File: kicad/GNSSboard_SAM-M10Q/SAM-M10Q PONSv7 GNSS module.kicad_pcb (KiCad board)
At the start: 2 copper layers, 34 x 16 mm, 8 parts, among them J1 2005280040, U2 SAM-M10Q-00B

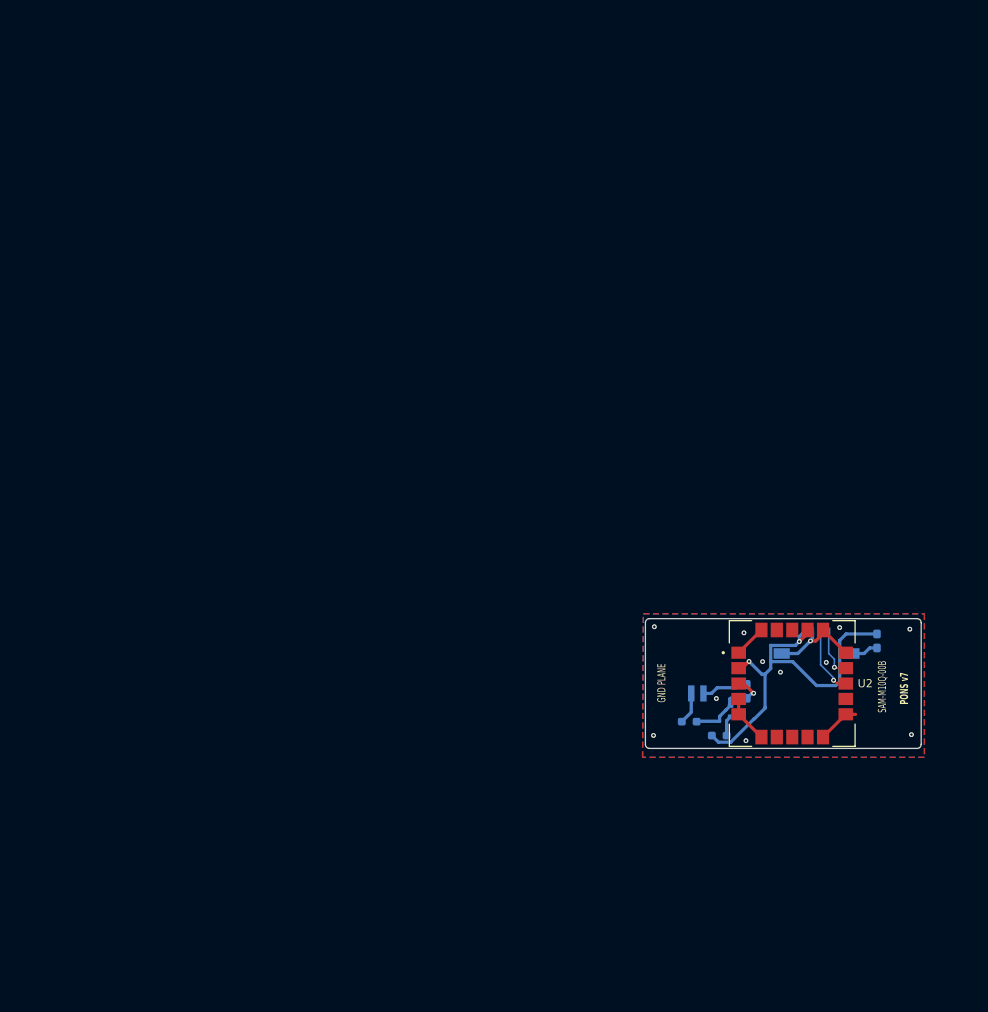
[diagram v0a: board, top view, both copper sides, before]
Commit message: 0.986 新基板（SCH16T 外付け）の kicad を追加し、ガーバー出力を git から外した
kicad/IMU_murata/ — SCH16T-K01-10 のブレイクアウト（新規）
本体の J7（Molex 200528-0080・8pin FPC）へ 1:1 ケーブルで繋ぐ外付け基板。
J1 のピン順を本体 J7 と一致させてある（1=+3V3 2=RESET 3=MOSI 4=CS 5=SCK
6=SYNC 7=MISO 8=GND）。シンボルとフットプリントも同梱。
- ★ R2（CS-GND の 4.7k）は実装しない。CS は負論理なので、プルダウンすると
  MCU が駆動していない間セレクト状態になる。R1（EXTRESN プルアップ）は実装する
- 本体側の GPIO 割り当ては settings.h の SCH16T_PIN_* が正本
  （一覧は docs/imu_sch16t_plan.md §3）

mainboard / GNSS モジュールの更新
- mainboard: DisplayModule_PONSv7 の pcb / pro / sch、MS5611BNO085.kicad_sch、
  SHT_RP2354B.kicad_sch
- GNSS モジュール: pcb / pro / sch、および QRv7 と FPC 4p のフットプリントを
  同プロジェクトの Footprints/ へ取り込み

kicad/FPC/ を畳んだ
FPC コネクタ 1 個のためのプロジェクトだったので、フットプリントを
kicad/GNSSboard_SAM-M10Q/Footprints/ へ移して削除した。
中身は同じで、差分は KiCad が再生成する uuid だけ。

ガーバー・ドリルのプロット出力を git から外した
kicad/.gitignore に追加（*.gbr *.gbl *.gbs *.gbp *.gbo *.gm1 *.gtl *.gts
*.gtp *.gto *.drl と、保険の *plot/ *plot.zip）。発注のたびに作り直せるうえ、
基板を直すたびに巨大な差分になる（ルート .gitignore の production/ と同じ理由）。
★ 入れ物のフォルダ名で書かないこと。v5_1plot/ のような名前は付け方が毎回違うので
  次の基板で外れる。既存の *-backups/ / *.kicad_prl と同じ方針。

Co-Authored-By: Claude Opus 5 <noreply@anthropic.com>
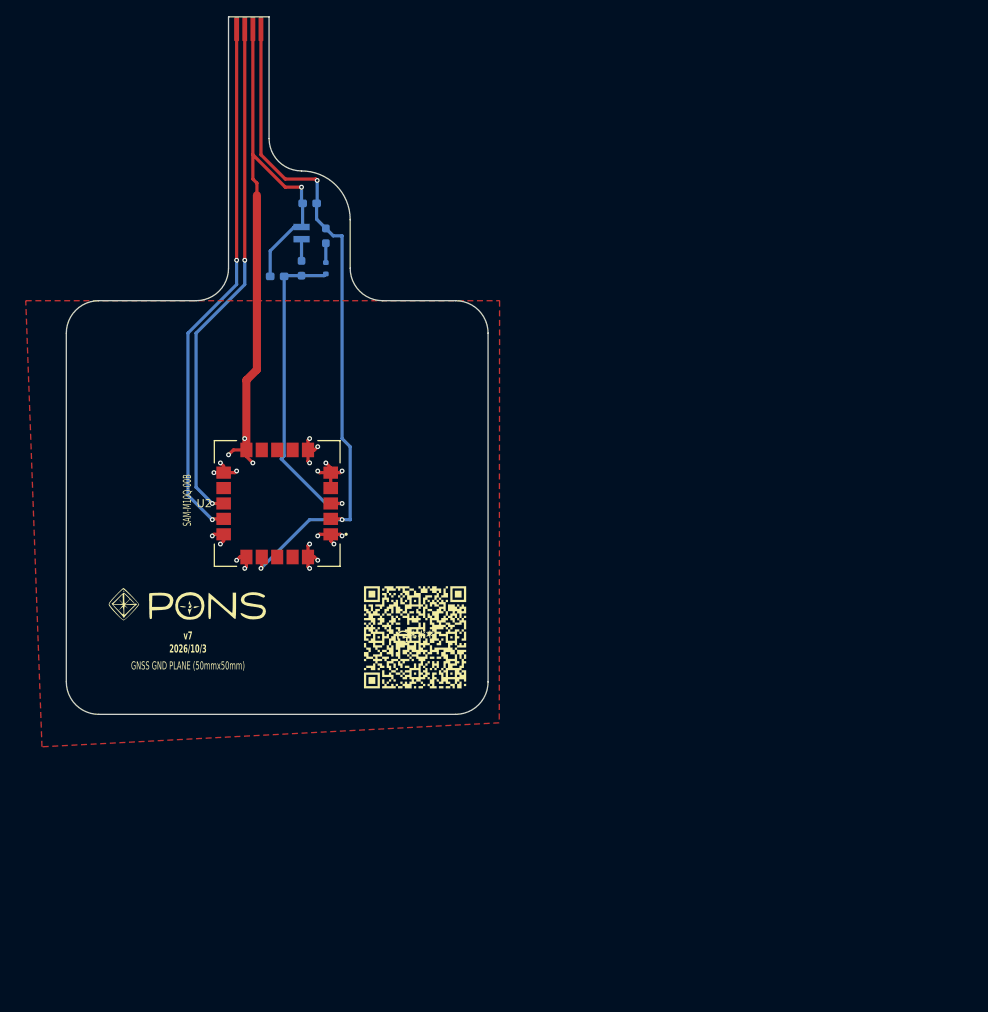
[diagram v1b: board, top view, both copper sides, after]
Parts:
- removed J1: 2005280040, Connector_FFC-FPC:Molex_200528-0040_1x04-1MP_P1.00mm_Horizontal
- added G***: LOGO, 2005280040:QRv7, F.Cu at (101.0, 93.5)
- added G***: LOGO, 2005280040:PONS_logo, F.Cu at (73.0, 89.5)
- added J2: Conn_01x04, GPS_TFT:FPC_CON 4p 1mm, F.Cu at (80.5, 18.5)
- moved C2 88.3 mm to (88.0, 40.0), turned to 180 degrees
- moved R1 78.4 mm to (90.0, 44.0), turned to 90 degrees
- moved C3 77.3 mm to (84.0, 49.0), turned to 180 degrees
- moved BT1 74.9 mm to (87.0, 43.7), turned to 0 degrees
- moved D1 74.0 mm to (90.0, 48.0), turned to 90 degrees
- moved R2 73.6 mm to (87.0, 48.0), turned to -90 degrees
- moved U2 67.3 mm to (84.0, 77.0), turned to 180 degrees
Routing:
- net GND: track 35.3 -> 109.9 mm, vias 12 -> 23
- net GNSS_RX: track 6.43 -> 65.7 mm, vias 1 -> 2
- net GNSS_TX: track 8.33 -> 63.2 mm, vias 1 -> 2
- net +3.3V: track 48.7 -> 85.2 mm, vias 2 -> 3
- net V_BCKUP: track 11.8 -> 39.9 mm
- net Net-(BT1-+): track 3.96 -> 2.67 mm
- removed copper zone on B.Cu, net GND
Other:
- board size 34 x 16 mm -> 52 x 86 mm
- board text added: "GNSS GND PLANE (50mmx50mm)"
- board text added: "SAM-M10Q 0.1uF x2 Resistor x2 MS621FE x1"
- board text added: "Stiffener 1/2: At Gold finger Total thickness 0.3mm PI Backside"
- board text added: "Stiffener 2/2: At GND plate. Total thickness 0.3mm PI Backside"
- board text added: "Total 2 stiffeners"
- board text added: "v7 2026/10/3"
- board text removed: "GND PLANE"
- board text removed: "PONS v7"
- board text removed: "SAM-M10Q SH connector 4P x2 Molex connector 0.1uF x2 Resistor x2"
- board text removed: "基板向き 前倒し"

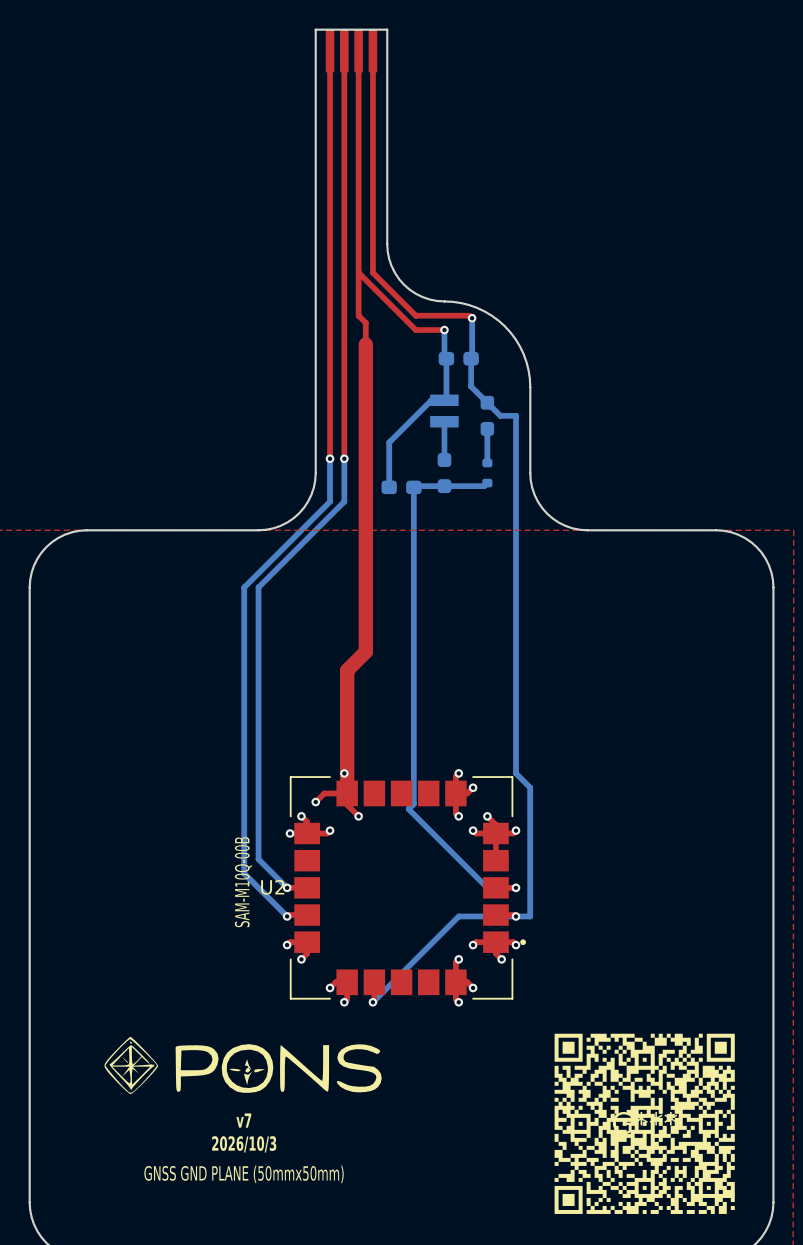
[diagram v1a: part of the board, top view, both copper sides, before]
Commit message: 0.993 v7.1 基板の回路図と PCB を仕上げ、SW OFF のままの充電と電源異常を画面と音声で知らせるようにした
- power.cpp（新規）: USB の判定を usb_power_present() に一本化（v7.1 は VBUS を
  GPIO47 の ADC で測る）。電源経路の異常（2026-10-15 の充電 IC 焼損）を検出し、
  地図の POWER FAULT!! と power_fault.wav（30 秒ごと・最低音量 60）で知らせる。
  受信機は LINK_ST_PWR_FAULT を受けてトーン（同じ音声だとボートへの指示に聞こえる）
- v7.1: SW を OFF にしたまま USB で充電していると満充電にならない（Q3 のボディ
  ダイオード経由）。SW4 の OFF 側が GPIO40 を GND に落とすのを読み、地図に注意を出し
  1 度だけ読み上げる（charge_sw_off / charge_sw_on。排他グループ WAV_EXCL_CHARGE_SW）。
  移動中・ミラー中・リプレイ中・デモ中は出さない。判定に USB を入れない
  （VBUS が一瞬 4.3V を割ると 0V が本物の電池電圧として流れるため）。このあいだは
  電池低下の警告を止め、無線は RHAVE_VOLT を立てず LINK_ST_USB_SW_OFF、CSV は空欄
- 受信モードの電池表示を s55r42 の形に。SW OFF のまま USB の側は s5V / r5V
- backlight.cpp（新規）: v7.1 のバックライト PWM と VEML7700 の自動調光。
  飛行 CSV に lux / backlight 列
- E220 の M0/M1 は v7.1 で GPIO31 へ（GPIO47 は USB_SENS）
- 本体の回路図・PCB: SCH16T の J6 を逆順に（完成済みの FPC で J6-n ↔ J3-(9-n)）、
  F1 0805L035 → 0805L050（夏の充電で切れない）、R34/R35 を 10k/5.1k、C32 を 10µF 0805、
  SPI1 の SCK/MOSI/CS に 33Ω（R49〜R51）、スライドスイッチを MST-12D18G2 に、
  回路図とつながらない旧フットプリント（C33/R37/R38/R11 470Ω）を削除、DNP の BOM 除外、
  CUS-12TB の残骸とライブラリ登録を削除、メモの部品番号を v7.1 に
- GNSS 基板を 5 ピン（V_BCKUP）に。バックアップ電池は本体へ移した
- case_cover（照度センサー VEML7700）の kicad を追加。IMU ブレイクアウトの R2 を DNP
- 音声 3 本（power_fault / charge_sw_off / charge_sw_on）は macOS の音声合成の仮音声
- docs/pons_power.md（新規）。README の「自作の手順」を v7.1 に書き直し、
  SCH16T の配線の記述（J7・1:1 ケーブル）を J6・逆順に直した
- gen_wav_flash.py はコメント中の引用符付きの音声名も拾うので、録音前の名前を書かない

PONS_BOARD は V7 と V71 の両方でビルド OK（3,929,776 / 3,923,504 B）/
gen_wav_flash.py --check は 35 ファイル一致 / 本体 PCB の DRC は未配線 0・回路図と一致
（シルクの 6 件はボタンと USB の突起で意図どおり）/ GNSS 基板も未配線 0 / 実機は未確認

Co-Authored-By: Claude Opus 5.5 <noreply@anthropic.com>
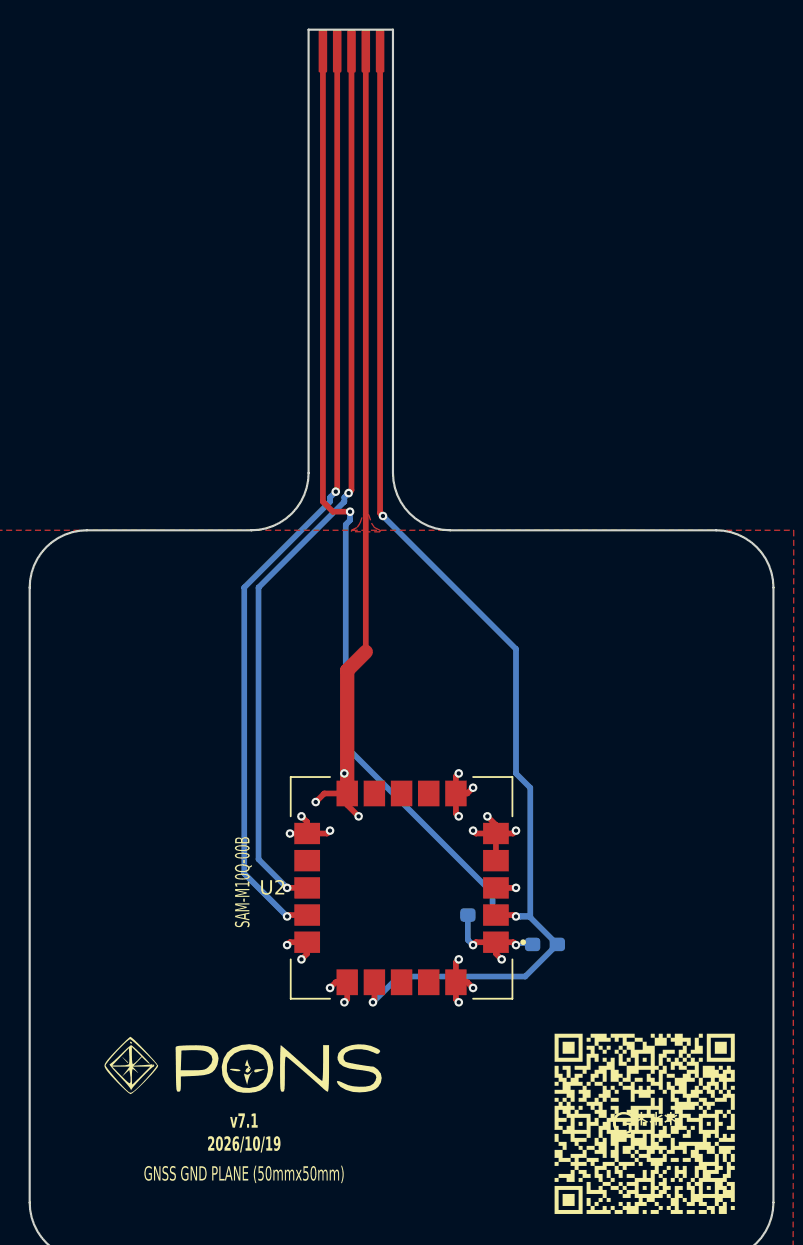
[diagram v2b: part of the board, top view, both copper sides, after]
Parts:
- removed BT1: MS621FE, Battery:BatteryHolder_Seiko_MS621F
- removed D1: RB520S-30, Diode_SMD:D_SOD-523
- removed R1: 220, Resistor_SMD:R_0603_1608Metric_Pad0.98x0.95mm_HandSolder
- removed R2: 470, Resistor_SMD:R_0603_1608Metric_Pad0.98x0.95mm_HandSolder
- J2: footprint GPS_TFT:FPC_CON 4p 1mm -> GPS_TFT:FPC_CON 5p 1mm
- moved C2 41.4 mm to (94.0, 81.0)
- moved C3 30.4 mm to (89.5, 78.9)
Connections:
- J2 pad 1: GNSS_RX -> V_BCKUP
- J2 pad 2: GNSS_TX -> GNSS_RX
- J2 pad 3: GND -> GNSS_TX
- J2 pad 4: +3.3V -> GND
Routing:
- net V_BCKUP: track 39.9 -> 70.3 mm, vias 1 -> 2
- net GND: track 109.9 -> 92.3 mm, vias 23 -> 22
- net Net-(BT1-+): track 2.67 -> 0.00 mm
- net Net-(D1-A): track 2.39 -> 0.00 mm
- net +3.3V: track 85.2 -> 87.5 mm
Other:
- outline, holes or cut-outs redrawn
- board text added: "v7.1 2026/10/19"
- board text removed: "v7 2026/10/3"

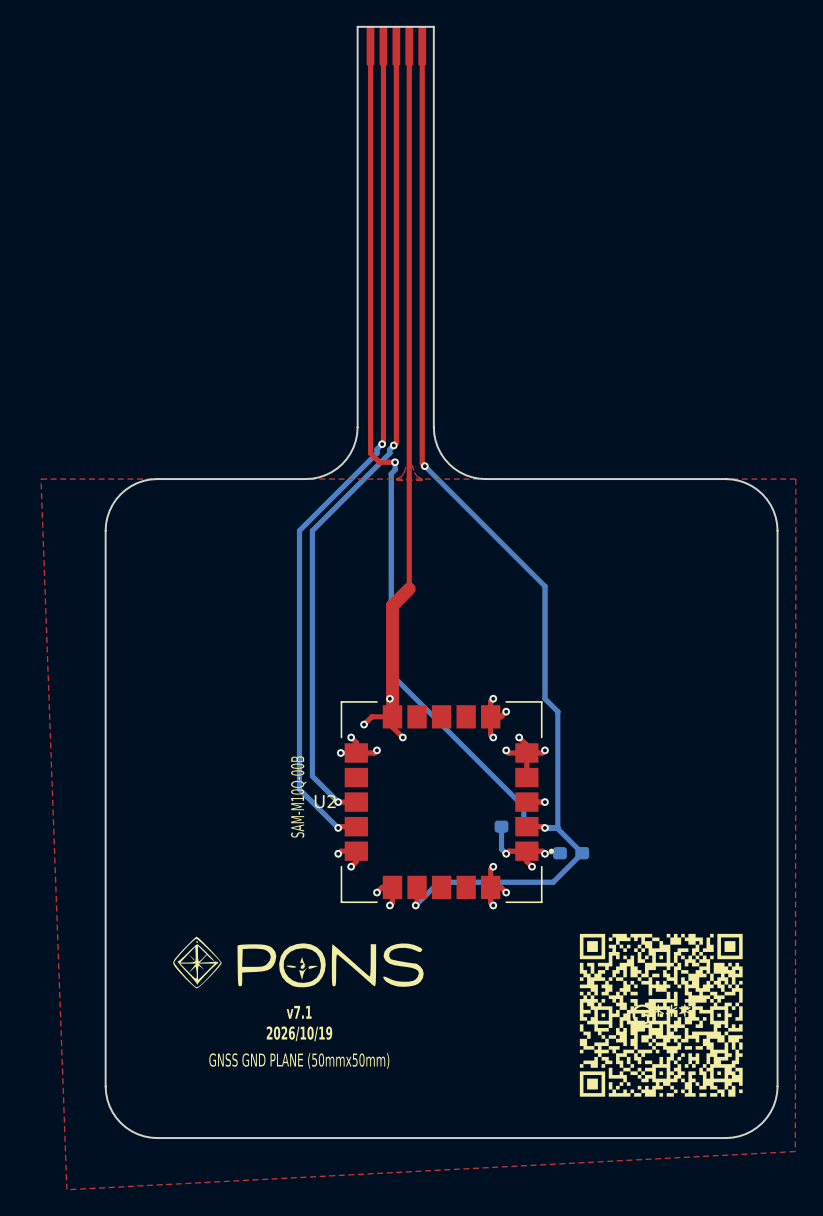
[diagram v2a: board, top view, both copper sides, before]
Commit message: 0.994 GNSS の翌日起動を速くし、本番前チェック・高温充電の警告・電池低下の点滅を入れ、v7.1 基板の逆接保護と発注前の修正を仕上げた
- GNSS: AssistNow Autonomous を有効化（CFG-VALSET で RAM と BBR。settings.h の
  GNSS_USE_ANA。0 でも OFF を書き込む＝BBR に残った ON を消すため）。前日と同じ時間帯の
  起動が 23〜28 秒 → 3〜4 秒（BT1 が生きていること）。NAV-AOPSTATUS を 1Hz で受け、
  GNSS DETAIL 3 に ANA:ON data/use/calc、log.txt に「... after boot」（TTFF）・最初の
  測位の軌道の出どころ・10 分ごとの計算時間。ACK 待ちの間も imu_service_if_due() を
  呼ぶ（以前からの抜け）
- readiness.cpp（新規）: 本番前チェック。GNSS・IMU・ESKF・較正（マウント外れだけ。
  日付またぎは推測なので入れない＝台の上での APPLY を促さない）・地上の姿勢・設定画面の
  赤丸・USB・電池 50%・SD・無線（送信モード）がそろい、地上で止まっていたら 1 度だけ
  「準備完了」（ready.wav）。欠けていれば設定画面の右上に項目名。受信モード・リプレイ・
  デモは対象外。既存の判定を読むだけで、条件は書き写さない
- 高温での充電の警告（v7・v7.1）: USB 接続中に MS5611 が 45°C を 30 秒超え続けたら
  地図に TOO HOT TO CHARGE と charge_hot.wav（60 秒ごと・最低音量 60）。電池の仕様は
  充電 0〜45°C。地図の段は電源異常と共用（異常 ＞ 高温 ＞ SW OFF）
- 電池低下のときの点滅（v7.1）: 電池低下の警告と同じ 3.5V でバックライトを 2 秒点灯・
  4 秒消灯。3.65V か USB で戻る（3.5V で戻すと入り切りをくり返す）。消灯中も本来の
  明るさは追い続ける（照度追従の立ち上がりで 2 秒の点灯が暗くならないように）
- 本体の回路図・PCB: 電池の逆接保護 Q4（AO3401A、D が電池側）＋ R52、PWR1 の
  ネットを VBAT_RAW に。C32 を 10µF 0805 に（10/20 に直したのが 0402 に戻っていた）。
  D5 を RB751S40（逆流が少ない。PCBA で実装）に。古いメモを整理
- IMU 基板の GND が IC1.16・C3 だけ分かれていたのをつないだ。J3 の値を 01x08 に。
  case_cover の部品番号を回路図と一致。GNSS 基板の裏面を GND ベタに（浮いていた
  19 個のビアがつながった）
- 音声 2 本（ready / charge_hot）は macOS の音声合成の仮音声
- docs: pons_power.md に Q4・P-ch FET 3 段の役割・電池の保護回路（DTP603048(PHR) の
  仕様書）・R39 を 2.2kΩ に戻さない理由（電池の最大充電 430mA も超える）・高温の警告・
  電池低下の点滅。README に GNSS の起動・本番前チェック・新しい警報・v7.1 の USB-C と
  充電時間、古い記述（v7 の実結線試験・無線の立ち上げ手順書の冒頭）を今の状態に。
  CLAUDE.md に BBR に書いた GNSS 設定が残る件と readiness.cpp
- kicad/.gitignore に *.pos

PONS_BOARD は V7 と V71 の両方でビルド OK（4,052,376 / 4,046,728 B）/
gen_wav_flash.py --check は 37 ファイル一致 / 本体 PCB の DRC は未配線 0・回路図と一致
（シルクの 6 件は意図どおり）/ IMU・カバー・GNSS 基板も未配線 0・回路図と一致 /
BOM の LCSC 番号は全 48 種類を JLC/LCSC の部品情報と照合 / 実機は未確認

Co-Authored-By: Claude Opus 5.5 <noreply@anthropic.com>
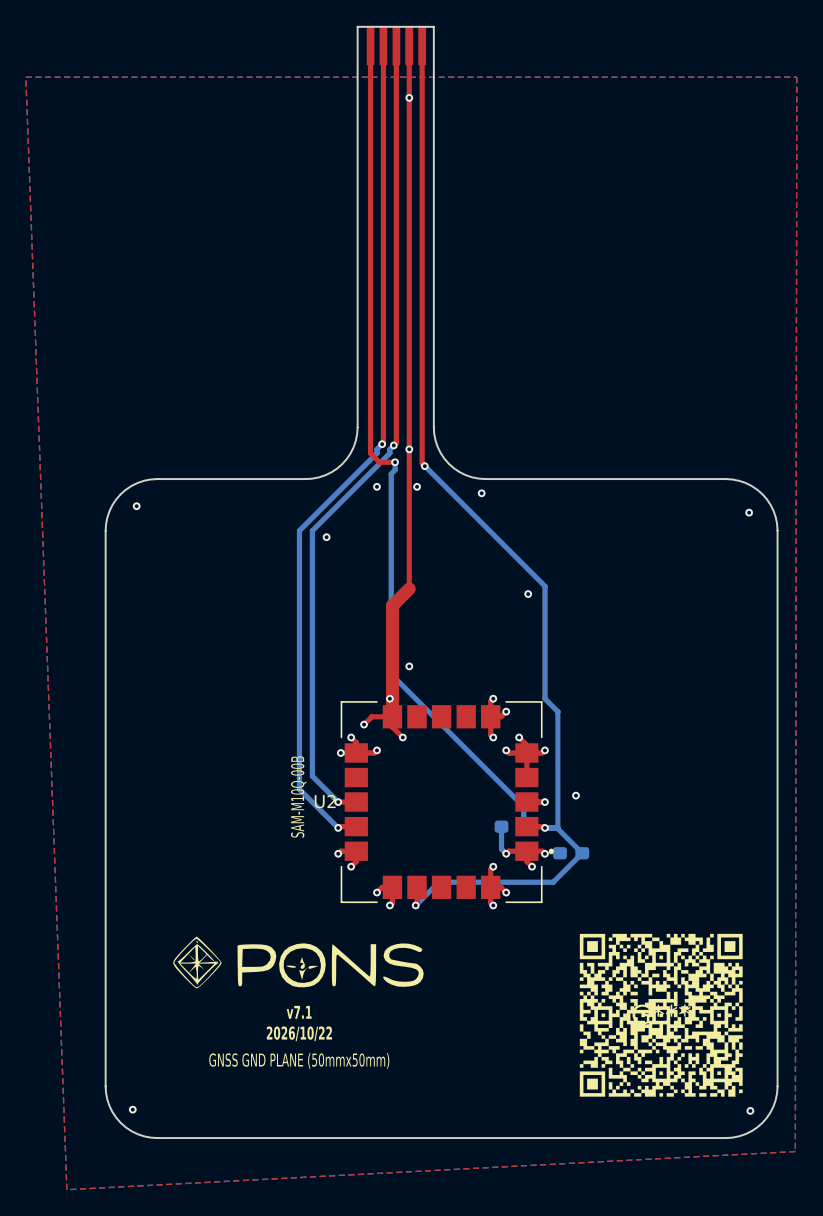
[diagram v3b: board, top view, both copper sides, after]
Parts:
- J2: value Conn_01x04 -> Conn_01x05
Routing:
- net GND: vias 22 -> 35
- added copper zone on B.Cu, net GND
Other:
- board text added: "v7.1 2026/10/22"
- board text removed: "v7.1 2026/10/19"
